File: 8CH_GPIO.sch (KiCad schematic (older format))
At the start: 1 part

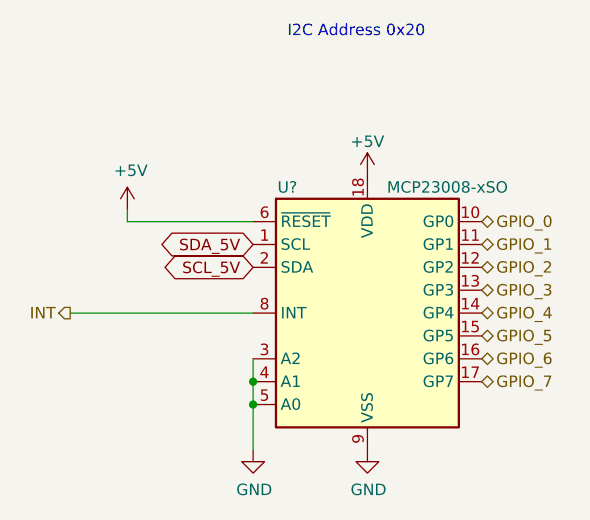
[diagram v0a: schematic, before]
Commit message: Updated Schematic to correct power page
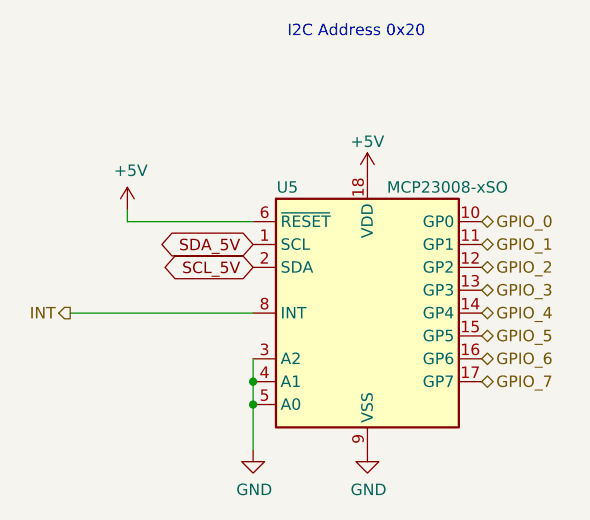
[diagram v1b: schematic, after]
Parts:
- gave numbers to parts that had none: 1
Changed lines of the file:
@@
 $EndDescr
 $Comp
-L power:GND #PWR?
+L power:GND #PWR0161
 U 1 1 5FD30180
 P 5200 4200
-F 0 "#PWR?" H 5200 3950 50  0001 C CNN
+F 0 "#PWR0161" H 5200 3950 50  0001 C CNN
 F 1 "GND" H 5205 4027 50  0000 C CNN
 F 2 "" H 5200 4200 50  0001 C CNN
@@
 $EndComp
 $Comp
-L power:+5V #PWR?
+L power:+5V #PWR0162
 U 1 1 5FD30777
 P 5200 3000
-F 0 "#PWR?" H 5200 2850 50  0001 C CNN
+F 0 "#PWR0162" H 5200 2850 50  0001 C CNN
 F 1 "+5V" H 5200 3150 50  0000 C CNN
 F 2 "" H 5200 3000 50  0001 C CNN
@@
 SCL_5V
 $Comp
-L power:GND #PWR?
+L power:GND #PWR0163
 U 1 1 5FD3227F
 P 4700 4200
-F 0 "#PWR?" H 4700 3950 50  0001 C CNN
+F 0 "#PWR0163" H 4700 3950 50  0001 C CNN
 F 1 "GND" H 4705 4027 50  0000 C CNN
 F 2 "" H 4700 4200 50  0001 C CNN
@@
 I2C Address 0x20
 $Comp
-L Interface_Expansion:MCP23008-xSO U?
+L Interface_Expansion:MCP23008-xSO U5
 U 1 1 5FD6B453
 P 5200 3600
-F 0 "U?" H 4850 4150 50  0000 C CNN
+F 0 "U5" H 4850 4150 50  0000 C CNN
 F 1 "MCP23008-xSO" H 5550 4150 50  0000 C CNN
 F 2 "Package_SO:SOIC-18W_7.5x11.6mm_P1.27mm" H 5200 2550 50  0001 C CNN
@@
 	4700 4000 4700 4200
 $Comp
-L power:+5V #PWR?
+L power:+5V #PWR0182
 U 1 1 5FD743BB
 P 4150 3150
-F 0 "#PWR?" H 4150 3000 50  0001 C CNN
+F 0 "#PWR0182" H 4150 3000 50  0001 C CNN
 F 1 "+5V" H 4165 3323 50  0000 C CNN
 F 2 "" H 4150 3150 50  0001 C CNN
